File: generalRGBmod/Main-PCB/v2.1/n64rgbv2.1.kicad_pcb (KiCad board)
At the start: 2 copper layers, 61.2 x 32.8 mm, 89 parts, among them J11 SolderJumper_3_Open, J12 SolderJumper_3_Open, J2 SolderJumper_2_Open, J21 SolderJumper_2_Open, J3 Conn_02x05_Odd_Even, J31 SolderJumper_2_Open, U1 EPM570T100, U2 ADV7125, U3 TSH122ICT, U4 TLV70018_SOT23-5, U5 TLV70033_SOT23-5

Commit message: incremental improvements after first prototype run
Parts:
- removed FB6: Ferrite_Bead_Small, Resistor_SMD:R_0603_1608Metric
- added SHIELD_FINGER1: S1761-42R, individual_footprints:Pad_4.5_3.0, B.Cu at (121.9, 103.1)
- C1, C2, C3, C31, C33, C34, C4, C5, C6: footprint Capacitor_SMD:C_0805_2012Metric -> Capacitor_SMD:C_0805_2012Metric_Pad1.15x1.40mm_HandSolder
- C10, C11, C12, C13, C14, C15, C16, C17, C18, C19, C20, C21, C22, C23, C24, C25, C27, C28, C32, C41, C42, C51, C52: footprint Capacitor_SMD:C_0603_1608Metric -> Capacitor_SMD:C_0603_1608Metric_Pad1.05x0.95mm_HandSolder
- FB1, FB2, FB3, FB4, FB5: value Ferrite_Bead_Small -> MPZ1608S221ATA00; footprint Resistor_SMD:R_0603_1608Metric -> Resistor_SMD:R_0603_1608Metric_Pad1.05x0.95mm_HandSolder
- J3: value Conn_02x05_Odd_Even -> 30310-6002HB
- R10, R11, R12, R13, R2, R21, R22, R31, R32, R33, R34: footprint Resistor_SMD:R_0603_1608Metric -> Resistor_SMD:R_0603_1608Metric_Pad1.05x0.95mm_HandSolder
- U4, U5: footprint Package_TO_SOT_SMD:SOT-23-5 -> Package_TO_SOT_SMD:SOT-23-5_HandSoldering
- moved FB4 1.32 mm to (138.2, 90.0)
- moved R33 1.16 mm to (150.4, 89.9)
- moved R32 1.12 mm to (150.4, 91.9)
- moved J31 0.77 mm to (146.8, 89.8)
- moved R31 0.74 mm to (146.8, 91.9)
- moved C13 0.51 mm to (145.5, 100.6)
- moved C21 0.47 mm to (157.5, 105.3)
- moved C20 0.47 mm to (157.5, 103.8)
- moved C28 0.47 mm to (166.2, 97.0)
- moved R21 0.46 mm to (163.0, 97.0)
- moved R34 0.45 mm to (167.9, 97.0)
- moved C27 0.45 mm to (164.7, 97.0)
- moved R22 0.44 mm to (161.4, 97.0)
- moved C15 0.18 mm to (134.7, 104.0)
- moved FBN11 0.12 mm to (124.1, 103.4)
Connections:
- U1 pad 92: Net-(U1-Pad92) -> Filter_Bypass
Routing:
- net Filter_Bypass: track 8.57 -> 34.1 mm
- net /~CSYNC_75_pre: track 11.0 -> 10.0 mm
- net Net-(C27-Pad1): track 6.33 -> 7.07 mm
- net /~CSYNC: track 27.0 -> 27.8 mm
- net +5VA: track 98.0 -> 98.8 mm
- net D6_i: track 8.95 -> 9.45 mm
- net GNDD: track 15.4 -> 15.0 mm, vias 31 -> 33
- net GND: track 31.7 -> 31.4 mm, vias 33 -> 32
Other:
- board text added: "GND Finger"
- board text added: "N64RGBv2.1.20200405"
- board text removed: "N64RGBv2.1.20200317"

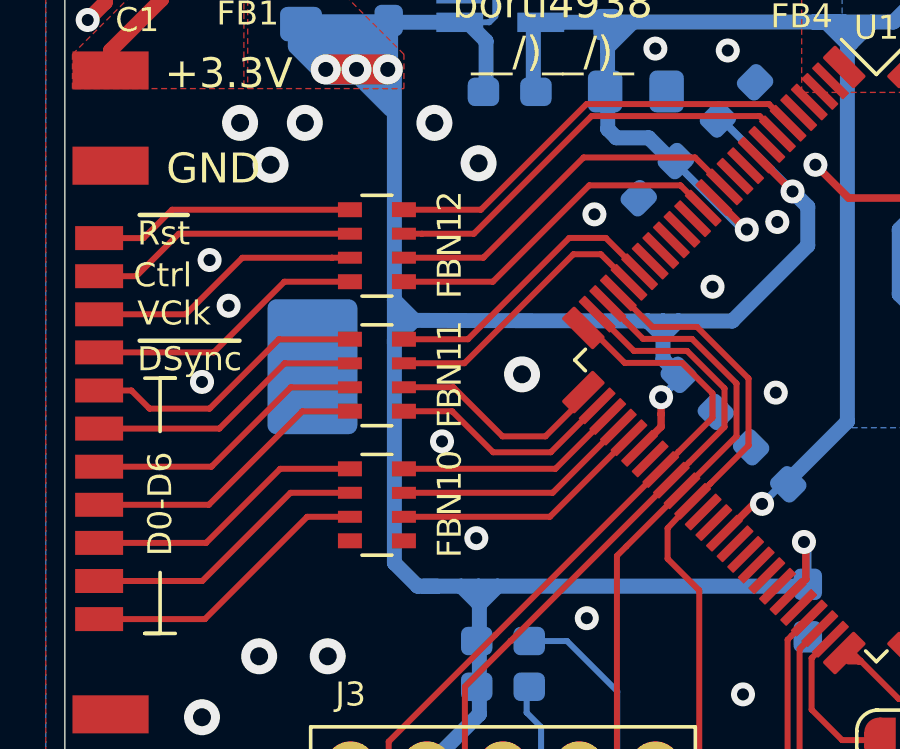
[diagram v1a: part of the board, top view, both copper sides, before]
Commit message: update BOM for new flex cable concept
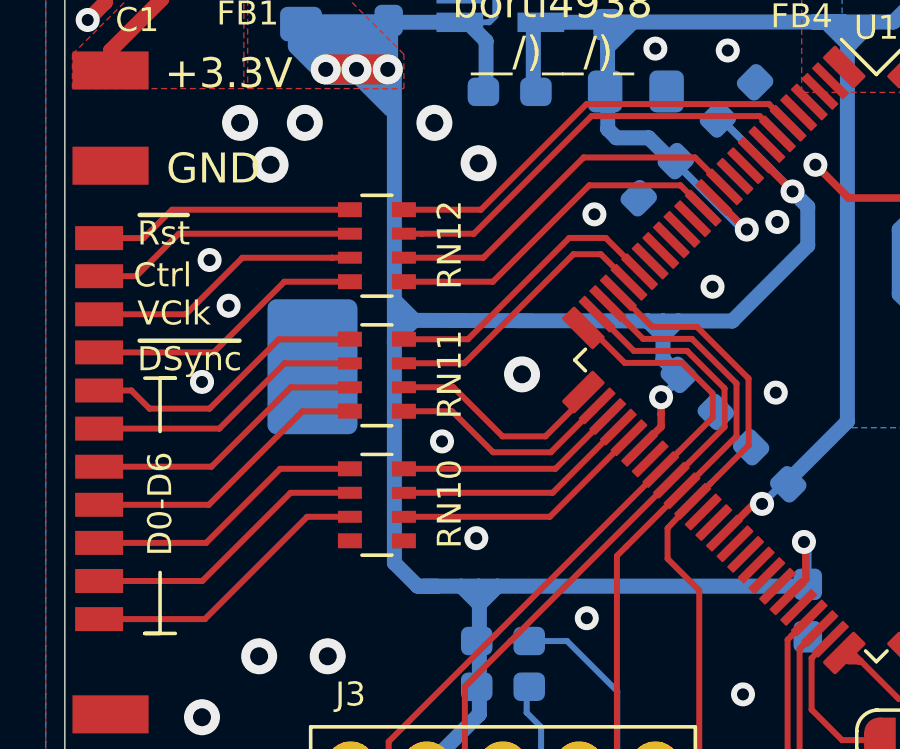
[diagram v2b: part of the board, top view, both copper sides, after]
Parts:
- RN10: renamed from FBN10; value BLA31BD221SN4D -> CAT16-47R0F4LF / CAY16-47R0F4LF
- RN11: renamed from FBN11; value BLA31BD221SN4D -> CAT16-47R0F4LF / CAY16-47R0F4LF
- RN12: renamed from FBN12; value BLA31BD221SN4D -> CAT16-47R0F4LF / CAY16-47R0F4LF

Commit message: remove auto deblur stuff from N64RGB - I found more and more situations where the auto detection does not work reliable - so I removed it for now
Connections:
- net /~15b_MODE renamed /en_IGR_Rst_Func
- net /~FORCE_VI_DB renamed /VIDeBlur_t
- net /~IT_SW renamed /en_IGR_DeBl_15b_Func
- net /~VI_DB renamed /~15b_mode_t

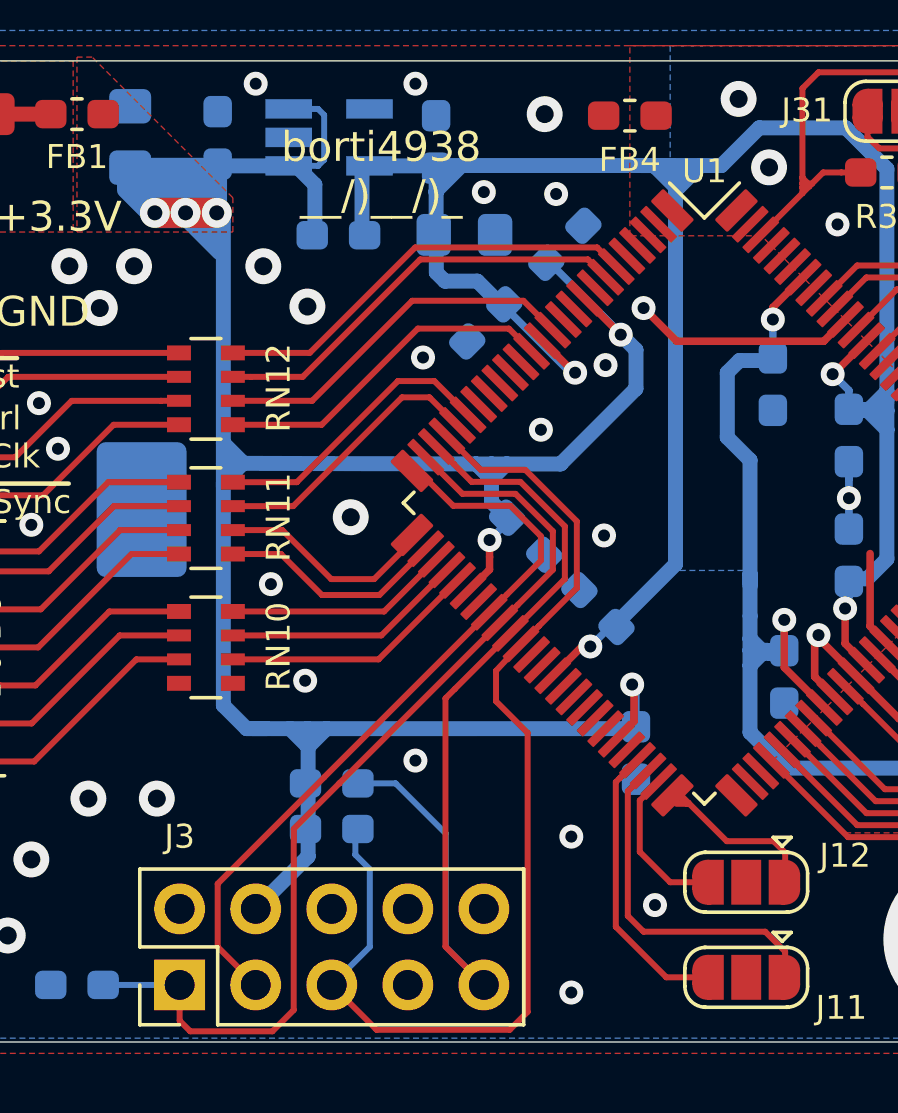
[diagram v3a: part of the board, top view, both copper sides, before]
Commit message: do not run JTAG through other pins as this may cause problem if used CPLDs are assembled
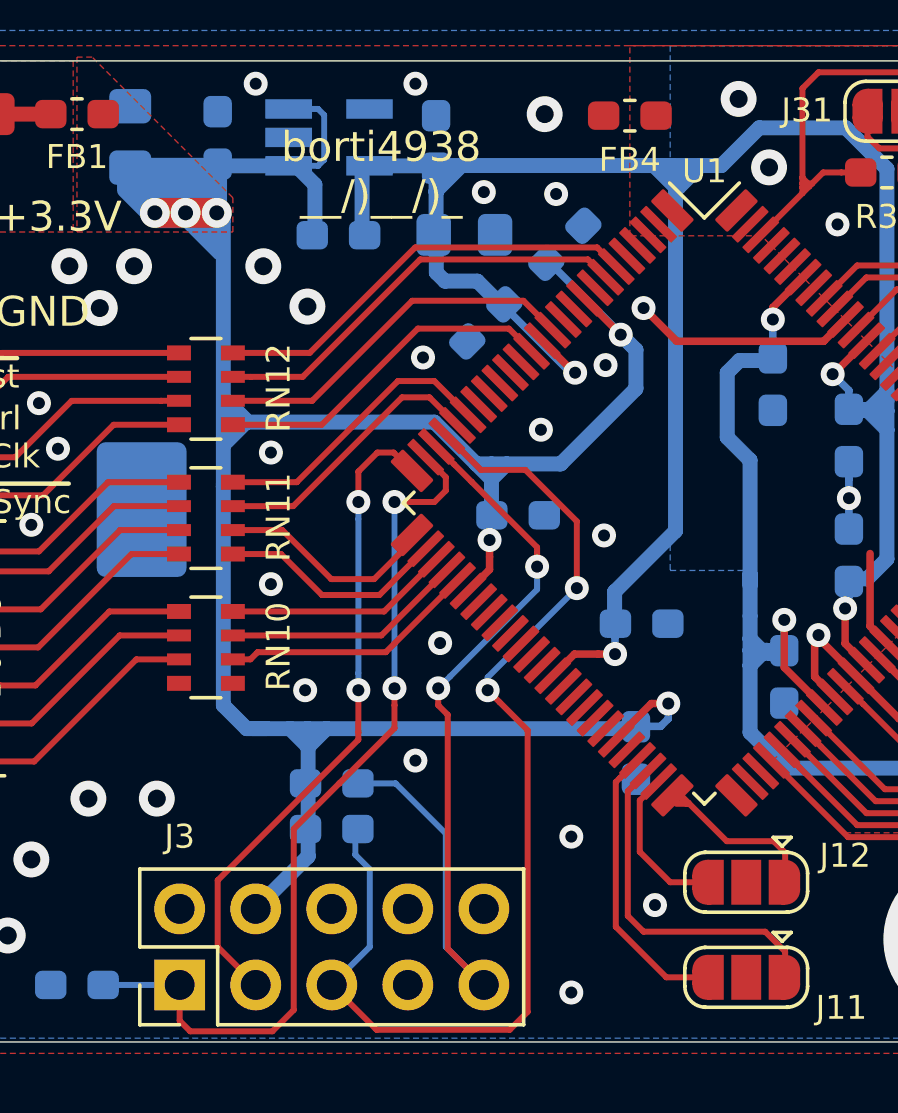
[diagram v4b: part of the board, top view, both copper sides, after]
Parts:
- moved C11 1.55 mm to (138.6, 106.9), turned to 0 degrees
- moved C15 0.74 mm to (134.5, 103.3), turned to 0 degrees
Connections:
- U1 pad 33: TDO -> Net-(U1-Pad33)
- U1 pad 34: TCK -> Net-(U1-Pad34)
- U1 pad 35: TDI -> Net-(U1-Pad35)
- U1 pad 36: TMS -> Net-(U1-Pad36)
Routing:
- net TCK: track 32.9 -> 29.7 mm, vias 0 -> 2
- net TDO: track 25.1 -> 21.9 mm, vias 0 -> 2
- net TDI: track 32.2 -> 30.7 mm, vias 0 -> 2
- net TMS: track 36.8 -> 37.0 mm, vias 0 -> 2
- net GNDD: vias 33 -> 34
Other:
- board text added: "N64RGBv2.1.20200809"
- board text removed: "N64RGBv2.1.20200405"
